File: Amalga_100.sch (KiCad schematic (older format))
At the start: 43 parts, among them P1 USB_B, P10 IN-, P2 Interface, P3 IN+, P4 IN-, P5 MOTOR3, P6 MOTOR2, P7 MOTOR1, P9 CONN_6-HSWR-V2-rescue

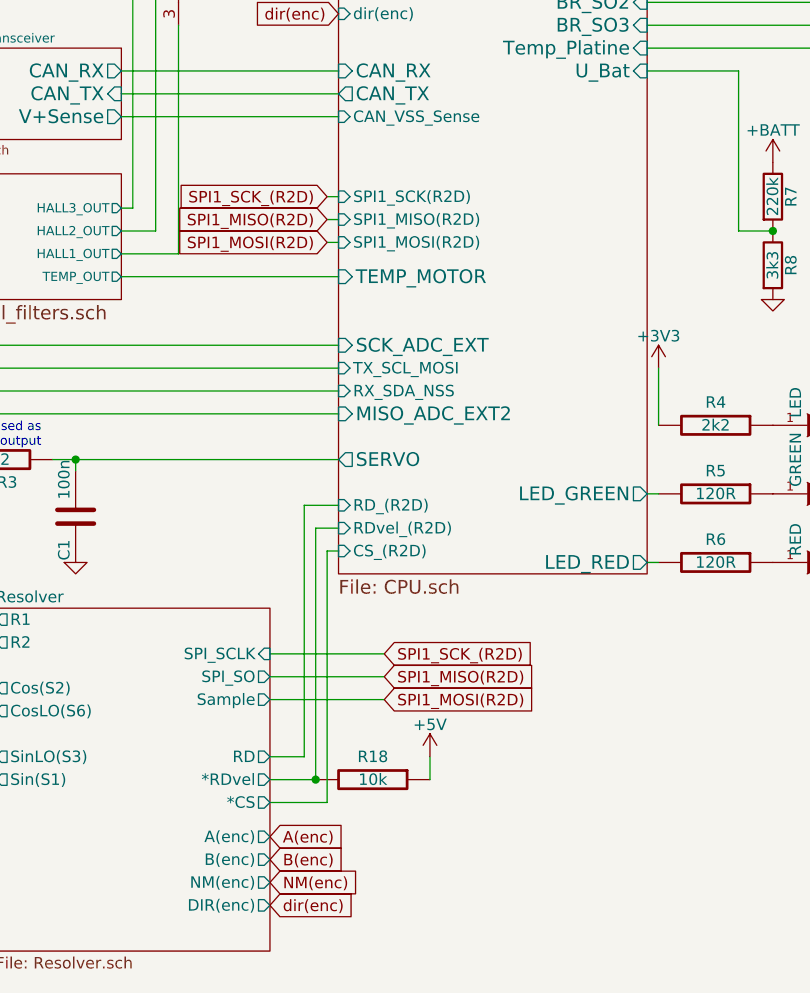
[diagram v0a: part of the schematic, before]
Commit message: -started implementing new sin/cos-Encoder Inputs -small changes like silkscreen
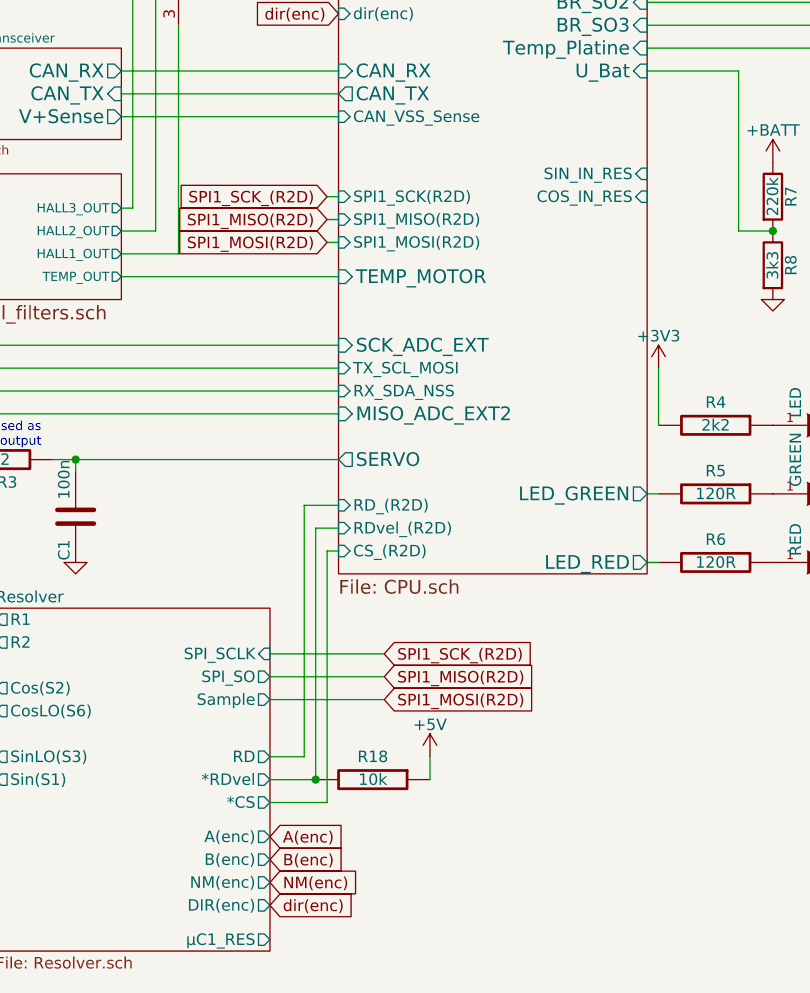
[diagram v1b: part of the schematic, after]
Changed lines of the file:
@@
 EESchema Schematic File Version 4
 LIBS:Amalga_100-cache
-EELAYER 29 0
+EELAYER 26 0
 EELAYER END
 $Descr A4 11693 8268
@@
 F37 "RD_(R2D)" I L 3300 5550 50
 F38 "dir(enc)" I L 3300 3400 50
+F39 "SIN_IN_RES" I R 4650 4100 50
+F40 "COS_IN_RES" I R 4650 4200 50
 $EndSheet
 Wire Wire Line
@@
 F16 "DIR(enc)" O R 3000 7300 50
 F17 "A(enc)" O R 3000 7000 50
+F18 "µC1_RES" O R 3000 7450 50
 $EndSheet
 Wire Wire Line

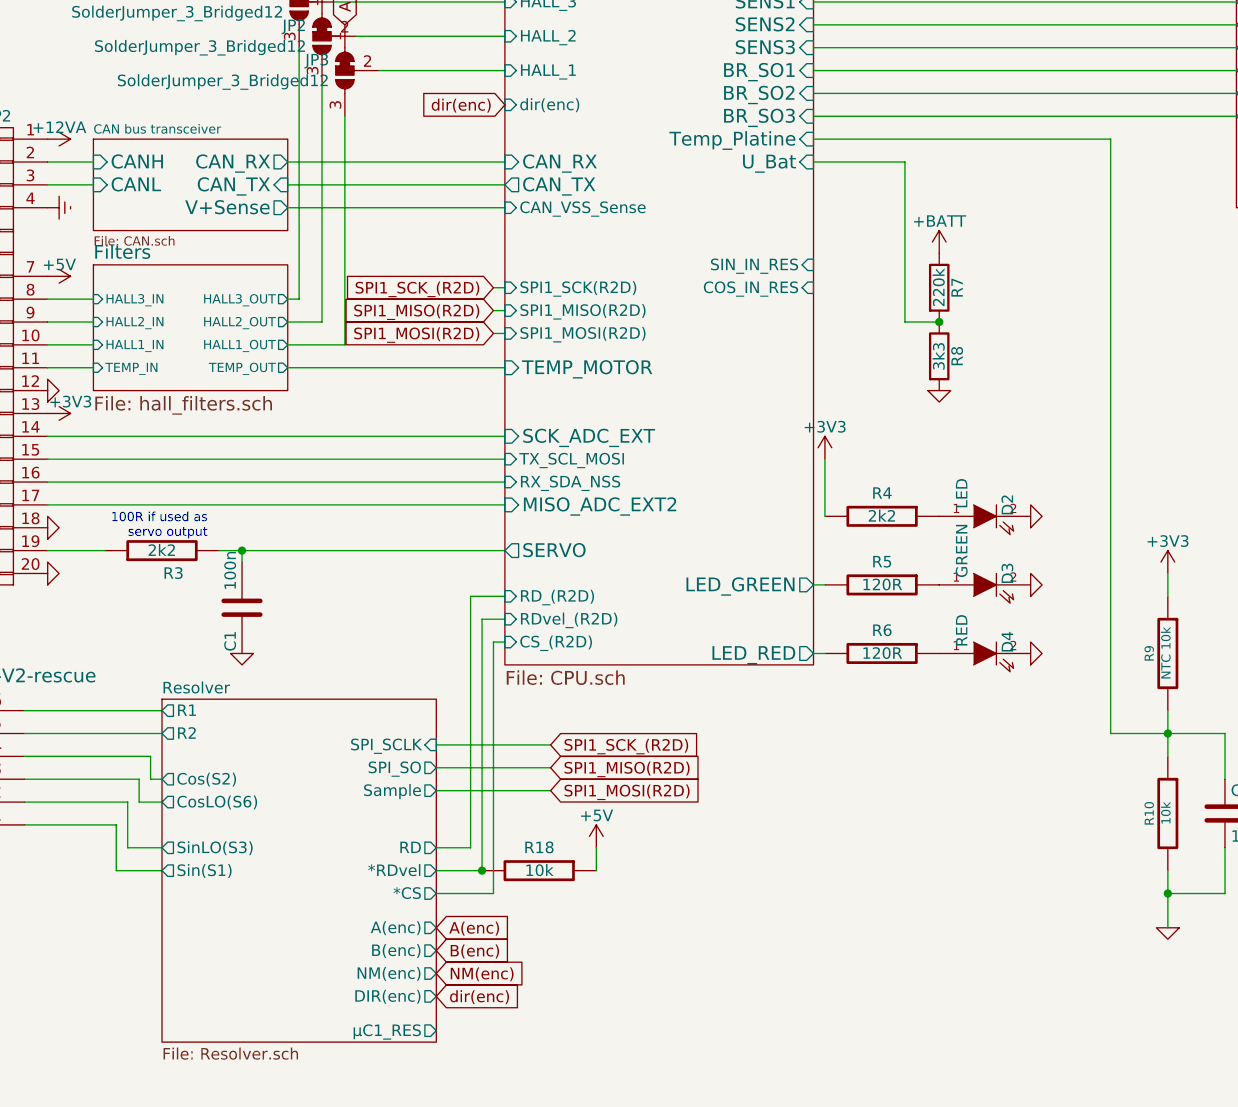
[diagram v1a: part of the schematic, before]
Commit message: added dc-bias for adc sin/cos resolver
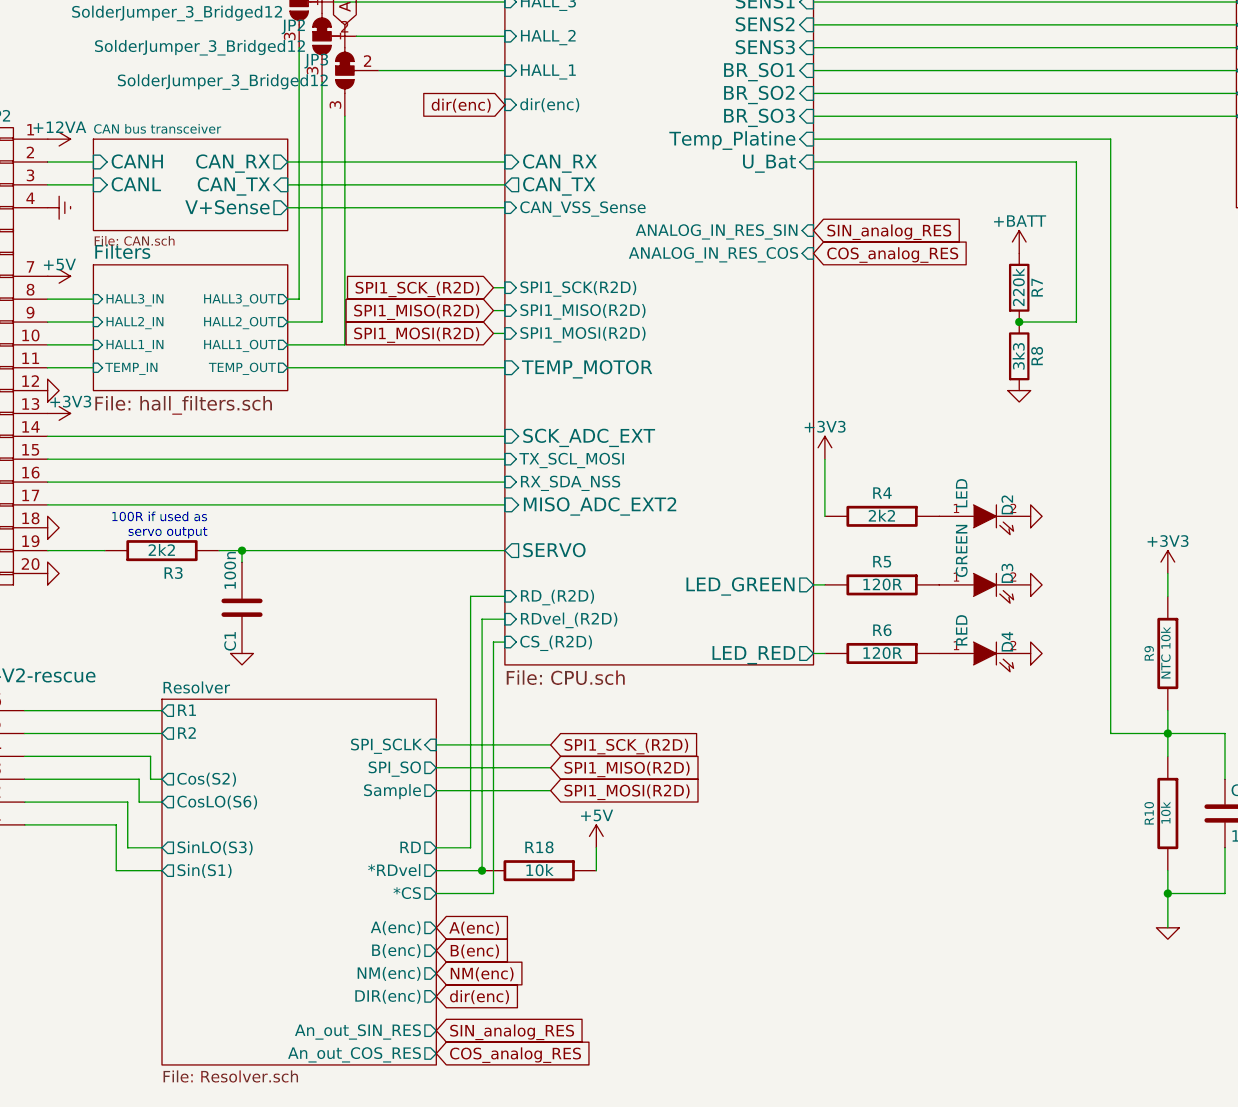
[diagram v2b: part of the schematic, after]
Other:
- moved on the sheet: R7, R8
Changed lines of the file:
@@
 L Amalga_100-rescue:+BATT-power #PWR03
 U 1 1 5895E69C
-P 5200 4050
-F 0 "#PWR03" H 5200 3900 50  0001 C CNN
-F 1 "+BATT" H 5200 4190 50  0000 C CNN
-F 2 "" H 5200 4050 60  0000 C CNN
-F 3 "" H 5200 4050 60  0000 C CNN
-	1    5200 4050
+P 5550 4050
+F 0 "#PWR03" H 5550 3900 50  0001 C CNN
+F 1 "+BATT" H 5550 4190 50  0000 C CNN
+F 2 "" H 5550 4050 60  0000 C CNN
+F 3 "" H 5550 4050 60  0000 C CNN
+	1    5550 4050
 	1    0    0    -1
 $EndComp
@@
 L Amalga_100-rescue:GND-RESCUE-BLDC_4-HSWR-V2-rescue #PWR04
 U 1 1 5895E69D
-P 5200 4650
-F 0 "#PWR04" H 5200 4650 30  0001 C CNN
-F 1 "GND" H 5200 4580 30  0001 C CNN
-F 2 "" H 5200 4650 60  0001 C CNN
-F 3 "" H 5200 4650 60  0001 C CNN
-	1    5200 4650
+P 5550 4650
+F 0 "#PWR04" H 5550 4650 30  0001 C CNN
+F 1 "GND" H 5550 4580 30  0001 C CNN
+F 2 "" H 5550 4650 60  0001 C CNN
+F 3 "" H 5550 4650 60  0001 C CNN
+	1    5550 4650
 	1    0    0    -1
 $EndComp
@@
 L Amalga_100-rescue:R-Device R7
 U 1 1 5895E69E
-P 5200 4200
-F 0 "R7" V 5280 4200 50  0000 C CNN
-F 1 "220k" V 5200 4200 50  0000 C CNN
-F 2 "Resistor_SMD:R_0805_2012Metric" V 5130 4200 30  0001 C CNN
-F 3 "" H 5200 4200 30  0000 C CNN
-	1    5200 4200
+P 5550 4200
+F 0 "R7" V 5630 4200 50  0000 C CNN
+F 1 "220k" V 5550 4200 50  0000 C CNN
+F 2 "Resistor_SMD:R_0805_2012Metric" V 5480 4200 30  0001 C CNN
+F 3 "" H 5550 4200 30  0000 C CNN
+	1    5550 4200
 	1    0    0    -1
 $EndComp
@@
 L Amalga_100-rescue:R-Device R8
 U 1 1 5895E69F
-P 5200 4500
-F 0 "R8" V 5280 4500 50  0000 C CNN
-F 1 "3k3" V 5200 4500 50  0000 C CNN
-F 2 "Resistor_SMD:R_0805_2012Metric" V 5130 4500 30  0001 C CNN
-F 3 "" H 5200 4500 30  0000 C CNN
-	1    5200 4500
-	1    0    0    -1
-$EndComp
-Connection ~ 5200 4350
+P 5550 4500
+F 0 "R8" V 5630 4500 50  0000 C CNN
+F 1 "3k3" V 5550 4500 50  0000 C CNN
+F 2 "Resistor_SMD:R_0805_2012Metric" V 5480 4500 30  0001 C CNN
+F 3 "" H 5550 4500 30  0000 C CNN
+	1    5550 4500
+	1    0    0    -1
+$EndComp
+Connection ~ 5550 4350
 $Comp
 L Amalga_100-rescue:+BATT-power #PWR05
@@
 	4650 3350 6500 3350
 Wire Wire Line
-	5200 4350 5050 4350
-Wire Wire Line
-	5050 4350 5050 3650
-Wire Wire Line
-	5050 3650 4650 3650
+	5550 4350 5800 4350
+Wire Wire Line
+	5800 4350 5800 3650
+Wire Wire Line
+	5800 3650 4650 3650
 Wire Wire Line
 	4650 3550 5950 3550
-Wire Wire Line
-	5950 3550 5950 6150
 $Comp
 L Amalga_100-rescue:+5V-power #PWR0101
@@
 F37 "RD_(R2D)" I L 3300 5550 50
 F38 "dir(enc)" I L 3300 3400 50
-F39 "SIN_IN_RES" I R 4650 4100 50
-F40 "COS_IN_RES" I R 4650 4200 50
+F39 "ANALOG_IN_RES_SIN" I R 4650 3950 50
+F40 "ANALOG_IN_RES_COS" I R 4650 4050 50
 $EndSheet
 Wire Wire Line
@@
 	1300 5350 1550 5350
 $Sheet
-S 1800 6000 1200 1500
+S 1800 6000 1200 1600
 U 5C9D0FFC
 F0 "Resolver" 50
@@
 F16 "DIR(enc)" O R 3000 7300 50
 F17 "A(enc)" O R 3000 7000 50
-F18 "µC1_RES" O R 3000 7450 50
+F18 "An_out_SIN_RES" O R 3000 7450 50
+F19 "An_out_COS_RES" O R 3000 7550 50
 $EndSheet
 Wire Wire Line
@@
 	1    0    0    -1
 $EndComp
+Text GLabel 3000 7450 2    50   Input ~ 0
+SIN_analog_RES
+Text GLabel 3000 7550 2    50   Input ~ 0
+COS_analog_RES
+Text GLabel 4650 3950 2    50   Input ~ 0
+SIN_analog_RES
+Text GLabel 4650 4050 2    50   Input ~ 0
+COS_analog_RES
+Wire Wire Line
+	5950 3550 5950 6150
 $EndSCHEMATC

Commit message: -changed ad2s1200 to ad2s1205  (pin compatibel) -changed excitation-buffer circuit. (AD8397 in use now) -fixed thermal-connections of planes
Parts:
- JP1, JP2, JP3: footprint Jumper:SolderJumper-3_P1.3mm_Bridged12_RoundedPad1.0x1.5mm -> Jumper:SolderJumper-3_P1.3mm_Open_RoundedPad1.0x1.5mm_NumberLabels
- R18: footprint Resistors_SMD:R_0805 -> Resistor_SMD:R_0805_2012Metric
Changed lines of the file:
@@
 EESchema Schematic File Version 4
 LIBS:Amalga_100-cache
-EELAYER 26 0
+EELAYER 29 0
 EELAYER END
 $Descr A4 11693 8268
@@
 F 0 "JP3" V 2554 3318 50  0000 L CNN
 F 1 "SolderJumper_3_Bridged12" V 2645 3318 50  0000 L CNN
-F 2 "Jumper:SolderJumper-3_P1.3mm_Bridged12_RoundedPad1.0x1.5mm" H 2600 3250 50  0001 C CNN
+F 2 "Jumper:SolderJumper-3_P1.3mm_Open_RoundedPad1.0x1.5mm_NumberLabels" H 2600 3250 50  0001 C CNN
 F 3 "~" H 2600 3250 50  0001 C CNN
 	1    2600 3250
@@
 F 0 "JP1" V 2354 3018 50  0000 L CNN
 F 1 "SolderJumper_3_Bridged12" V 2445 3018 50  0000 L CNN
-F 2 "Jumper:SolderJumper-3_P1.3mm_Bridged12_RoundedPad1.0x1.5mm" H 2400 2950 50  0001 C CNN
+F 2 "Jumper:SolderJumper-3_P1.3mm_Open_RoundedPad1.0x1.5mm_NumberLabels" H 2400 2950 50  0001 C CNN
 F 3 "~" H 2400 2950 50  0001 C CNN
 	1    2400 2950
@@
 F 0 "JP2" V 2454 3168 50  0000 L CNN
 F 1 "SolderJumper_3_Bridged12" V 2545 3168 50  0000 L CNN
-F 2 "Jumper:SolderJumper-3_P1.3mm_Bridged12_RoundedPad1.0x1.5mm" H 2500 3100 50  0001 C CNN
+F 2 "Jumper:SolderJumper-3_P1.3mm_Open_RoundedPad1.0x1.5mm_NumberLabels" H 2500 3100 50  0001 C CNN
 F 3 "~" H 2500 3100 50  0001 C CNN
 	1    2500 3100
@@
 F 0 "R18" V 3350 6750 50  0000 C CNN
 F 1 "10k" V 3450 6750 50  0000 C CNN
-F 2 "Resistors_SMD:R_0805" H 3450 6750 60  0001 C CNN
+F 2 "Resistor_SMD:R_0805_2012Metric" H 3450 6750 60  0001 C CNN
 F 3 "" H 3450 6750 60  0001 C CNN
 	1    3450 6750
